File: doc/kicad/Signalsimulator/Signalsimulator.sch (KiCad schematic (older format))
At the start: 12 parts, among them J1 Conn_02x03_Odd_Even

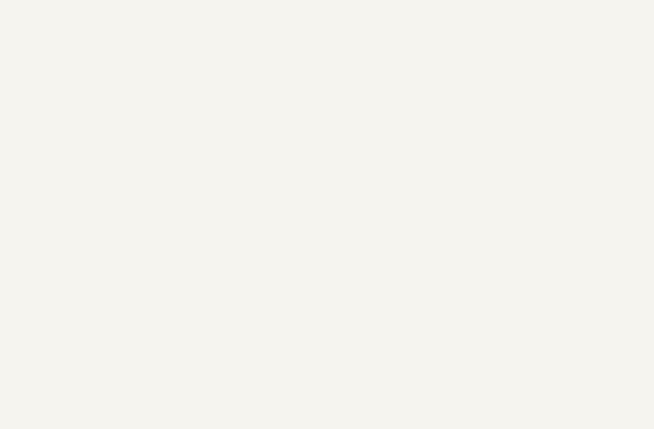
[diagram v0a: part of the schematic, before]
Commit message: Ecken rund gemacht, alle mit Montagelöcher
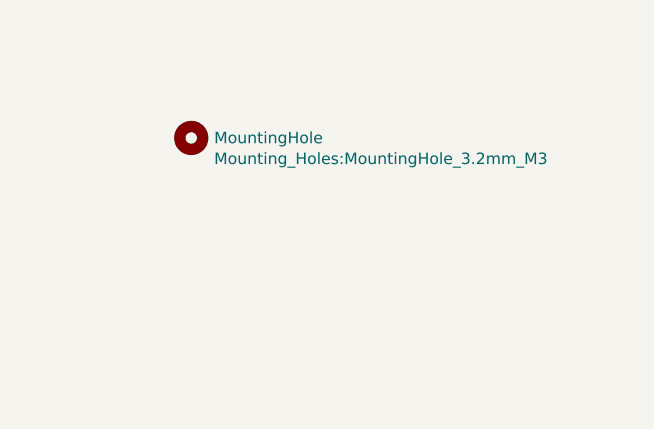
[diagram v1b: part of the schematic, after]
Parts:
- added H1: MountingHole, Mounting_Holes:MountingHole_3.2mm_M3, symbol Mechanical:MountingHole
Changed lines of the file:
@@
 Wire Wire Line
 	4250 2150 4700 2150
+$Comp
+L Mechanical:MountingHole H1
+U 1 1 608F4395
+P 7100 2450
+F 0 "H1" H 7200 2496 50  0001 L CNN
+F 1 "MountingHole" H 7200 2450 50  0000 L CNN
+F 2 "Mounting_Holes:MountingHole_3.2mm_M3" H 7200 2359 50  0000 L CNN
+F 3 "~" H 7100 2450 50  0001 C CNN
+	1    7100 2450
+	1    0    0    -1
+$EndComp
 $EndSCHEMATC

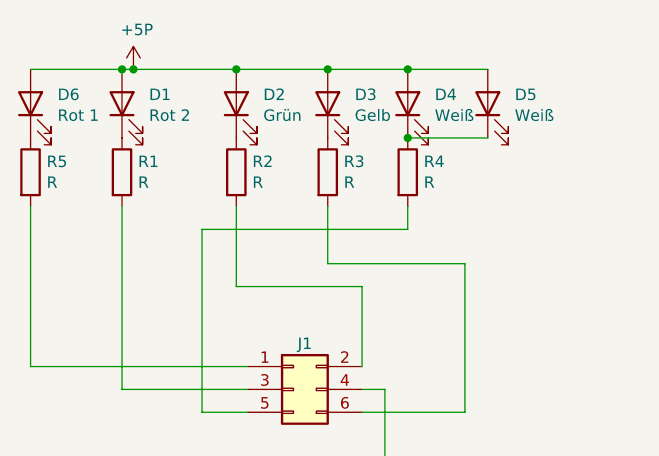
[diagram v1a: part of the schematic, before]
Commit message: Werte der Widerstände hinzugefügt
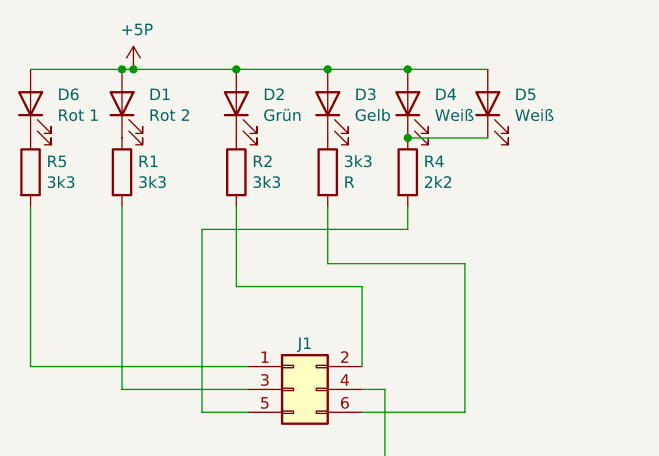
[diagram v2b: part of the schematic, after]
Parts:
- R1, R2, R5: value R -> 3k3
- R4: value R -> 2k2
- renumbered R3 to 3k3
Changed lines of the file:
@@
 P 4200 2600
 F 0 "R1" H 4270 2646 50  0000 L CNN
-F 1 "R" H 4270 2555 50  0000 L CNN
+F 1 "3k3" H 4270 2555 50  0000 L CNN
 F 2 "Resistors_THT:R_Axial_DIN0204_L3.6mm_D1.6mm_P7.62mm_Horizontal" V 4130 2600 50  0001 C CNN
 F 3 "~" H 4200 2600 50  0001 C CNN
@@
 P 4700 2600
 F 0 "R2" H 4770 2646 50  0000 L CNN
-F 1 "R" H 4770 2555 50  0000 L CNN
+F 1 "3k3" H 4770 2555 50  0000 L CNN
 F 2 "Resistors_THT:R_Axial_DIN0204_L3.6mm_D1.6mm_P7.62mm_Horizontal" V 4630 2600 50  0001 C CNN
 F 3 "~" H 4700 2600 50  0001 C CNN
@@
 P 5450 2600
 F 0 "R4" H 5520 2646 50  0000 L CNN
-F 1 "R" H 5520 2555 50  0000 L CNN
+F 1 "2k2" H 5520 2555 50  0000 L CNN
 F 2 "Resistors_THT:R_Axial_DIN0204_L3.6mm_D1.6mm_P7.62mm_Horizontal" V 5380 2600 50  0001 C CNN
 F 3 "~" H 5450 2600 50  0001 C CNN
@@
 $EndComp
 $Comp
-L Device:R R3
+L Device:R 3k3
 U 1 1 607A4631
 P 5100 2600
-F 0 "R3" H 5170 2646 50  0000 L CNN
+F 0 "3k3" H 5170 2646 50  0000 L CNN
 F 1 "R" H 5170 2555 50  0000 L CNN
 F 2 "Resistors_THT:R_Axial_DIN0204_L3.6mm_D1.6mm_P7.62mm_Horizontal" V 5030 2600 50  0001 C CNN
@@
 P 3800 2600
 F 0 "R5" H 3870 2646 50  0000 L CNN
-F 1 "R" H 3870 2555 50  0000 L CNN
+F 1 "3k3" H 3870 2555 50  0000 L CNN
 F 2 "Resistors_THT:R_Axial_DIN0204_L3.6mm_D1.6mm_P7.62mm_Horizontal" V 3730 2600 50  0001 C CNN
 F 3 "~" H 3800 2600 50  0001 C CNN
